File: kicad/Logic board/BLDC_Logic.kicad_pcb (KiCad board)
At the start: 2 copper layers, 43 parts, among them J1 CONN_01X03, J10 3v3 output, J11 SERIAL, J12 3 phase CTRL, J13 Programer, J14 IO, J2 CMD inputs, J3 CONN_01X03, J4 Pwr Input 5V, J5 5V output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

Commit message: continued layout work
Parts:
- moved R1 95.7 mm to (142.5, 82.5)
- moved R2 93.6 mm to (143.8, 59.7)
- moved J14 18.0 mm to (135.1, 133.6)
- moved C1 15.8 mm to (153.2, 115.6)
- moved C2 15.8 mm to (153.2, 120.4)
- moved Y1 14.7 mm to (157.5, 115.6)
- moved J7 13.2 mm to (181.4, 144.5)
- moved SW1 9.96 mm to (142.7, 74.9)
- moved J4 9.92 mm to (197.6, 142.2)
- moved R11 9.72 mm to (193.8, 98.3)
- moved R13 9.72 mm to (186.7, 103.4)
- moved R14 9.72 mm to (183.1, 105.9)
- moved R16 9.72 mm to (176.0, 111.0)
- moved R15 9.72 mm to (179.6, 108.5)
- moved J12 9.72 mm to (197.9, 111.0)
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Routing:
- net GND: track 279.5 -> 36.2 mm
- net Net-(J12-Pad4): track 38.5 -> 0.00 mm
- net Net-(J12-Pad6): track 38.5 -> 0.00 mm
- net Net-(J12-Pad5): track 38.5 -> 0.00 mm
- net Net-(J12-Pad3): track 38.5 -> 0.00 mm
- net Net-(J12-Pad2): track 38.5 -> 0.00 mm
- net Net-(J12-Pad1): track 38.0 -> 0.00 mm
- net Net-(J8-Pad3): track 36.3 -> 0.00 mm
- net Net-(J8-Pad2): track 36.3 -> 0.00 mm
- net Net-(J8-Pad1): track 36.3 -> 0.00 mm
- net Net-(J11-Pad1): track 35.5 -> 0.00 mm
- net Net-(J11-Pad2): track 35.5 -> 0.00 mm
- net Net-(R10-Pad1): track 43.3 -> 9.91 mm
- net Net-(R5-Pad1): track 39.0 -> 6.35 mm
- net Net-(R4-Pad1): track 34.1 -> 3.62 mm
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
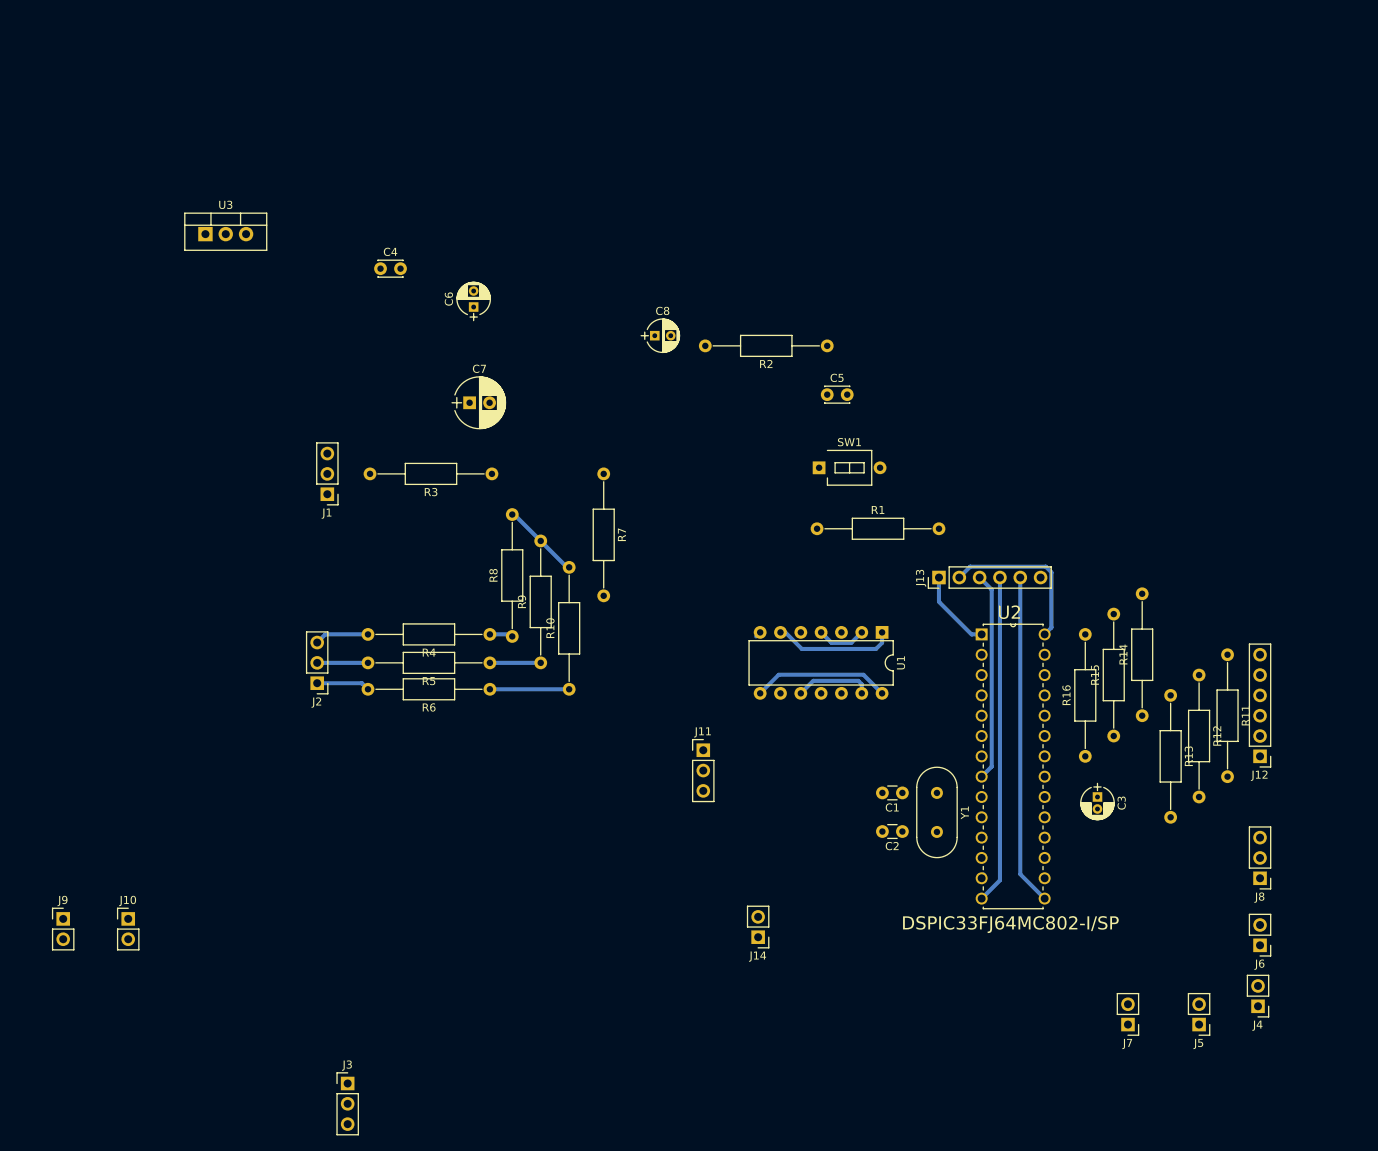
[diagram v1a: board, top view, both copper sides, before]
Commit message: Finished PCB switched 3ph board connector
completed the PCB layout of the board, changed from a 6 pole connect to
an 8 pole to intergrate 6 pwm signals and 5 volt power into one
connector, replacing the sperate 2 pole power connector. ( mountiong
holes are still needed
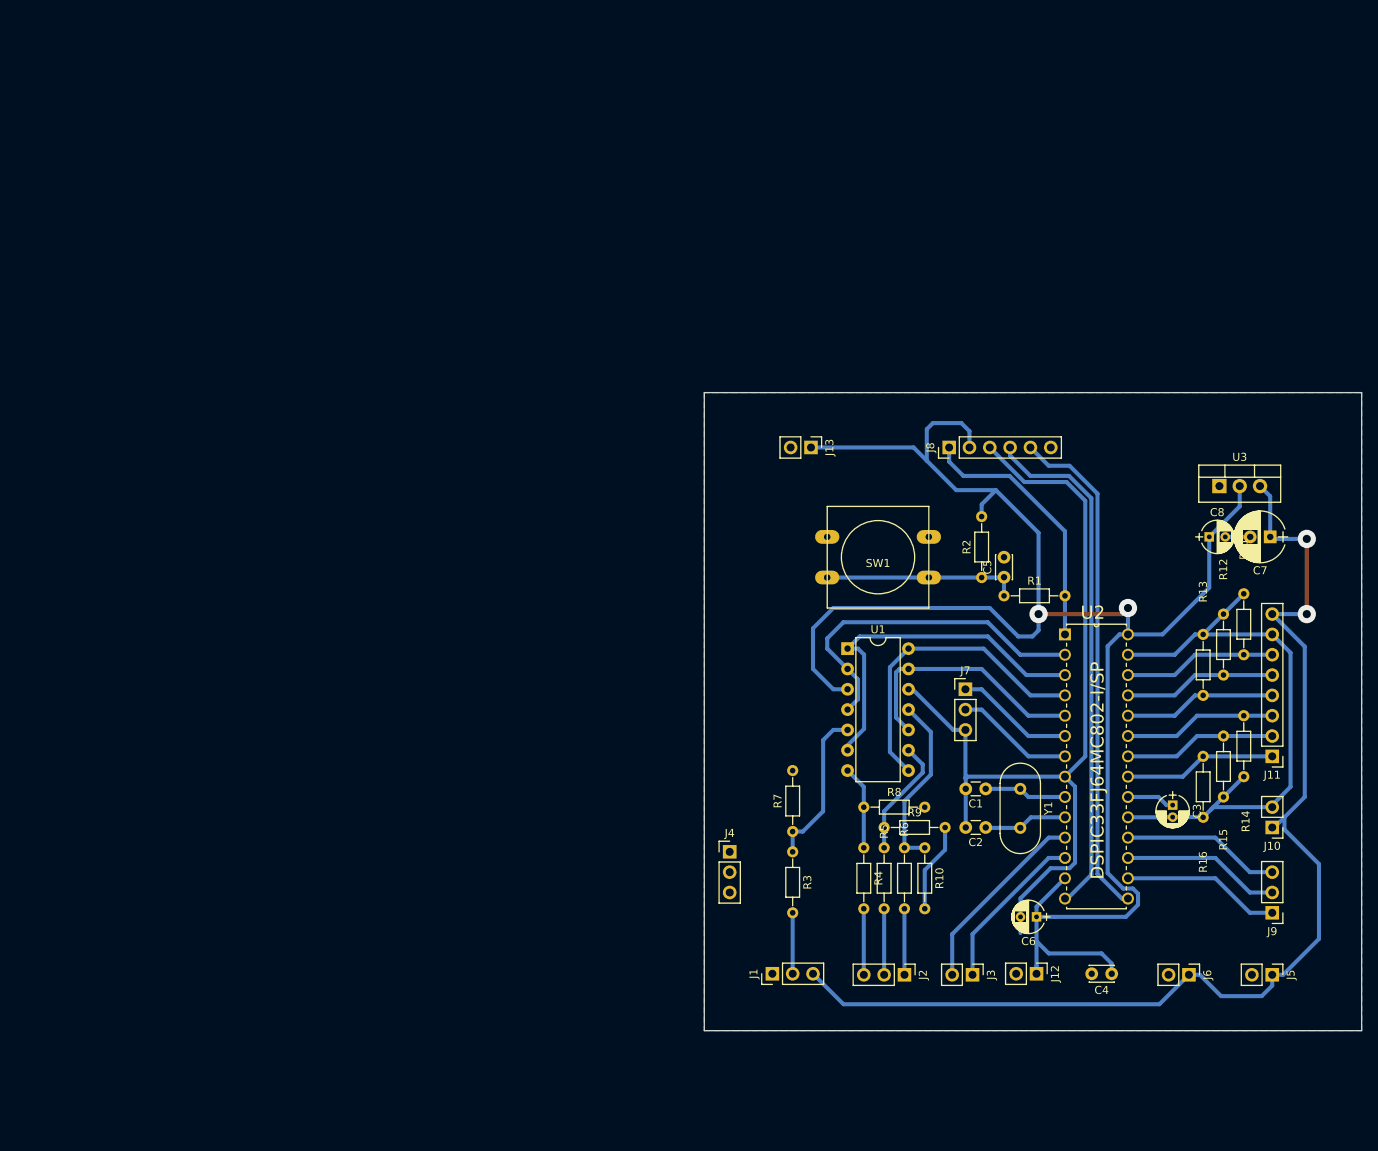
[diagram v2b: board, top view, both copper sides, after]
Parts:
- removed J14: IO, Pin_Headers:Pin_Header_Straight_1x02_Pitch2.54mm
- J10: value 3v3 output -> Encdr Pwr
- J11: value SERIAL -> 3ph board; footprint Pin_Headers:Pin_Header_Straight_1x03_Pitch2.54mm -> Pin_Headers:Pin_Header_Straight_1x08_Pitch2.54mm
- J12: value 3 phase CTRL -> 3v3 output; footprint Pin_Headers:Pin_Header_Straight_1x06_Pitch2.54mm -> Pin_Headers:Pin_Header_Straight_1x02_Pitch2.54mm
- J13: value Programer -> 3v3 output; footprint Pin_Headers:Pin_Header_Straight_1x06_Pitch2.54mm -> Pin_Headers:Pin_Header_Straight_1x02_Pitch2.54mm
- J3: value CONN_01X03 -> IO; footprint Pin_Headers:Pin_Header_Straight_1x03_Pitch2.54mm -> Pin_Headers:Pin_Header_Straight_1x02_Pitch2.54mm
- J4: value Pwr Input 5V -> CONN_01X03; footprint Pin_Headers:Pin_Header_Straight_1x02_Pitch2.54mm -> Pin_Headers:Pin_Header_Straight_1x03_Pitch2.54mm
- J7: value 5V output -> SERIAL; footprint Pin_Headers:Pin_Header_Straight_1x02_Pitch2.54mm -> Pin_Headers:Pin_Header_Straight_1x03_Pitch2.54mm
- J8: value Input -> Programer; footprint Pin_Headers:Pin_Header_Straight_1x03_Pitch2.54mm -> Pin_Headers:Pin_Header_Straight_1x06_Pitch2.54mm
- J9: value 3v3 output -> Encdr; footprint Pin_Headers:Pin_Header_Straight_1x02_Pitch2.54mm -> Pin_Headers:Pin_Header_Straight_1x03_Pitch2.54mm
- R1, R10, R11, R12, R13, R14, R15, R16, R2, R3, R4, R5, R6, R7, R8, R9: footprint Resistors_THT:R_Axial_DIN0207_L6.3mm_D2.5mm_P15.24mm_Horizontal -> Resistors_THT:R_Axial_DIN0204_L3.6mm_D1.6mm_P7.62mm_Horizontal
- SW1: footprint Buttons_Switches_THT:SW_DIP_x1_W7.62mm_Slide_LowProfile -> Buttons_Switches_THT:SW_PUSH-12mm
- moved J9 151.1 mm to (199.4, 130.6), turned to 180 degrees
- moved J10 143.5 mm to (199.4, 119.9), turned to 180 degrees
- moved U3 130.6 mm to (192.8, 77.2)
- moved C4 127.0 mm to (179.3, 138.2), turned to 180 degrees
- moved C6 103.7 mm to (169.9, 131.1), turned to 180 degrees
- moved C7 101.5 mm to (199.1, 83.6), turned to 180 degrees
- moved J2 82.0 mm to (153.4, 138.3), turned to 270 degrees
- moved J1 81.8 mm to (136.9, 138.2), turned to 90 degrees
- moved J3 79.3 mm to (161.9, 138.3), turned to 270 degrees
- moved C8 73.7 mm to (191.5, 83.6)
- moved J11 71.1 mm to (199.4, 111.0), turned to 180 degrees
- moved J4 68.8 mm to (131.6, 122.9), turned to 0 degrees
- moved J8 66.4 mm to (159.0, 72.4), turned to 90 degrees
- moved R3 60.4 mm to (139.4, 122.9), turned to 270 degrees
- moved R6 55.5 mm to (153.4, 122.4), turned to 270 degrees
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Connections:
- J10 pad 1: +3V3 -> +5V
- J11 pad 3: GND -> Net-(J11-Pad3)
- J12 pad 1: Net-(J12-Pad1) -> +3V3
- J12 pad 2: Net-(J12-Pad2) -> GND
- J13 pad 1: /MCLR -> +3V3
- J13 pad 2: +3V3 -> GND
- J3 pad 1: GND -> /IO2
- J3 pad 2: GND -> /IO1
- J4 pad 1: +5V -> GND
- J7 pad 1: +5V -> Net-(J7-Pad1)
- J7 pad 2: GND -> Net-(J7-Pad2)
- J8 pad 1: Net-(J8-Pad1) -> /MCLR
- J8 pad 2: Net-(J8-Pad2) -> +3V3
- J8 pad 3: Net-(J8-Pad3) -> GND
- J9 pad 1: +3V3 -> Net-(J9-Pad1)
- J9 pad 2: GND -> Net-(J9-Pad2)
- R11 pad 1: Net-(J12-Pad6) -> Net-(J11-Pad6)
- R12 pad 1: Net-(J12-Pad5) -> Net-(J11-Pad5)
- R13 pad 1: Net-(J12-Pad4) -> Net-(J11-Pad4)
- R14 pad 1: Net-(J12-Pad3) -> Net-(J11-Pad3)
- R15 pad 1: Net-(J12-Pad2) -> Net-(J11-Pad2)
- R16 pad 1: Net-(J12-Pad1) -> Net-(J11-Pad1)
- U2 pad 14: Net-(J13-Pad4) -> Net-(J8-Pad4)
- U2 pad 15: Net-(J13-Pad5) -> Net-(J8-Pad5)
- U2 pad 16: Net-(J8-Pad1) -> Net-(J9-Pad1)
- U2 pad 17: Net-(J8-Pad2) -> Net-(J9-Pad2)
- U2 pad 18: Net-(J8-Pad3) -> Net-(J9-Pad3)
- U2 pad 21: Net-(J12-Pad1) -> Net-(J11-Pad1)
- U2 pad 22: Net-(J12-Pad2) -> Net-(J11-Pad2)
- U2 pad 23: Net-(J12-Pad3) -> Net-(J11-Pad3)
- U2 pad 24: Net-(J12-Pad4) -> Net-(J11-Pad4)
- U2 pad 25: Net-(J12-Pad5) -> Net-(J11-Pad5)
- U2 pad 26: Net-(J12-Pad6) -> Net-(J11-Pad6)
- U2 pad 6: Net-(J11-Pad1) -> Net-(J7-Pad1)
- U2 pad 7: Net-(J11-Pad2) -> Net-(J7-Pad2)
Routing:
- net +3V3: track 21.1 -> 220.7 mm, vias 0 -> 2
- net GND: track 36.2 -> 196.9 mm
- net +5V: track 0.00 -> 143.7 mm, vias 0 -> 2
- net Net-(J8-Pad4): track 0.00 -> 65.0 mm
- net Net-(J8-Pad5): track 0.00 -> 63.4 mm
- net Net-(J13-Pad5): track 41.4 -> 0.00 mm
- net Net-(J13-Pad4): track 41.1 -> 0.00 mm
- net /O1: track 6.16 -> 43.3 mm
- net /O2: track 15.2 -> 45.0 mm
- net Net-(C5-Pad1): track 0.00 -> 24.4 mm
- net /IO1: track 0.00 -> 24.2 mm
- net /MCLR: track 10.1 -> 32.8 mm
- net /O4: track 10.1 -> 32.1 mm
- net /O3: track 17.5 -> 39.1 mm
- net /IO2: track 0.00 -> 20.6 mm
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- added copper zone on B.Cu, net GND
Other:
- board outline added: 82.2 x 79.8 mm

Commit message: add mounting holes change page size from A4 to Letter
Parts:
- added REF**: 1pin, Connectors:1pin, F.Cu at (131.8, 68.3)
- added REF**: 1pin, Connectors:1pin, F.Cu at (205.5, 68.3)
- added REF**: 1pin, Connectors:1pin, F.Cu at (131.8, 142.0)
- added REF**: 1pin, Connectors:1pin, F.Cu at (205.5, 142.0)
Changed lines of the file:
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@@
     (links 104)
     (no_connects 0)
-    (area 0 0 0 0)
+    (area 126.484667 64.249 210.641001 146.115)
     (thickness 1.6)
     (drawings 4)
     (tracks 254)
     (zones 0)
-    (modules 42)
+    (modules 46)
     (nets 36)
   )
-  (page A4)
+  (page USLetter)
   (layers
     (0 F.Cu signal)
@@
   )
   (setup
-    (last_trace_width 0.508)
+    (last_trace_width 0.25)
     (user_trace_width 0.508)
     (trace_clearance 0.254)
@@
     (mod_text_size 1 1)
     (mod_text_width 0.15)
-    (pad_size 1.524 1.524)
-    (pad_drill 0.762)
+    (pad_size 4.572 4.572)
+    (pad_drill 3.302)
     (pad_to_mask_clearance 0.2)
     (aux_axis_origin 0 0)
@@
     )
   )
+  (module Connectors:1pin (layer F.Cu)
+    (at 131.826 68.326)
+    (descr "module 1 pin (ou trou mecanique de percage)")
+    (tags DEV)
+    (fp_text reference REF** (at 0 -3.048) (layer F.SilkS)
+      (effects (font (size 1 1) (thickness 0.15)))
+    )
+    (fp_text value 1pin (at 0 3) (layer F.Fab)
+      (effects (font (size 1 1) (thickness 0.15)))
+    )
+    (fp_circle (center 0 0) (end 2 0.8) (layer F.Fab) (width 0.1))
+    (fp_circle (center 0 0) (end 2.6 0) (layer F.CrtYd) (width 0.05))
+    (fp_circle (center 0 0) (end 0 -2.286) (layer F.SilkS) (width 0.12))
+    (pad 1 thru_hole circle (at 0 0) (size 4.572 4.572) (drill 3.302) (layers *.Cu *.Mask))
+  )
+  (module Connectors:1pin (layer F.Cu)
+    (at 205.486 68.326)
+    (descr "module 1 pin (ou trou mecanique de percage)")
+    (tags DEV)
+    (fp_text reference REF** (at 0 -3.048) (layer F.SilkS)
+      (effects (font (size 1 1) (thickness 0.15)))
+    )
+    (fp_text value 1pin (at 0 3) (layer F.Fab)
+      (effects (font (size 1 1) (thickness 0.15)))
+    )
+    (fp_circle (center 0 0) (end 2 0.8) (layer F.Fab) (width 0.1))
+    (fp_circle (center 0 0) (end 2.6 0) (layer F.CrtYd) (width 0.05))
+    (fp_circle (center 0 0) (end 0 -2.286) (layer F.SilkS) (width 0.12))
+    (pad 1 thru_hole circle (at 0 0) (size 4.572 4.572) (drill 3.302) (layers *.Cu *.Mask))
+  )
+  (module Connectors:1pin (layer F.Cu)
+    (at 131.826 141.986)
+    (descr "module 1 pin (ou trou mecanique de percage)")
+    (tags DEV)
+    (fp_text reference REF** (at 0 -3.048) (layer F.SilkS)
+      (effects (font (size 1 1) (thickness 0.15)))
+    )
+    (fp_text value 1pin (at 0 3) (layer F.Fab)
+      (effects (font (size 1 1) (thickness 0.15)))
+    )
+    (fp_circle (center 0 0) (end 2 0.8) (layer F.Fab) (width 0.1))
+    (fp_circle (center 0 0) (end 2.6 0) (layer F.CrtYd) (width 0.05))
+    (fp_circle (center 0 0) (end 0 -2.286) (layer F.SilkS) (width 0.12))
+    (pad 1 thru_hole circle (at 0 0) (size 4.572 4.572) (drill 3.302) (layers *.Cu *.Mask))
+  )
+  (module Connectors:1pin (layer F.Cu)
+    (at 205.486 141.986)
+    (descr "module 1 pin (ou trou mecanique de percage)")
+    (tags DEV)
+    (fp_text reference REF** (at 0 -3.048) (layer F.SilkS)
+      (effects (font (size 1 1) (thickness 0.15)))
+    )
+    (fp_text value 1pin (at 0 3) (layer F.Fab)
+      (effects (font (size 1 1) (thickness 0.15)))
+    )
+    (fp_circle (center 0 0) (end 2 0.8) (layer F.Fab) (width 0.1))
+    (fp_circle (center 0 0) (end 2.6 0) (layer F.CrtYd) (width 0.05))
+    (fp_circle (center 0 0) (end 0 -2.286) (layer F.SilkS) (width 0.12))
+    (pad 1 thru_hole circle (at 0 0) (size 4.572 4.572) (drill 3.302) (layers *.Cu *.Mask))
+  )
   (gr_line (start 128.397 65.532) (end 128.397 145.288) (angle 90) (layer Edge.Cuts) (width 0.15))
